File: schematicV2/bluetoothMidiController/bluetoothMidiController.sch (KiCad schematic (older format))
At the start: 24 parts, among them SW10 G1, SW11 G#1, SW12 A1, SW13 A#1, SW14 B1, SW15 PWR, SW16 C2, SW17 ALT, SW2 OCT+, SW20 OCT-, SW3 C1, SW4 C#1, SW5 D1, SW6 D#1, SW7 E1, SW8 F1, SW9 F#1

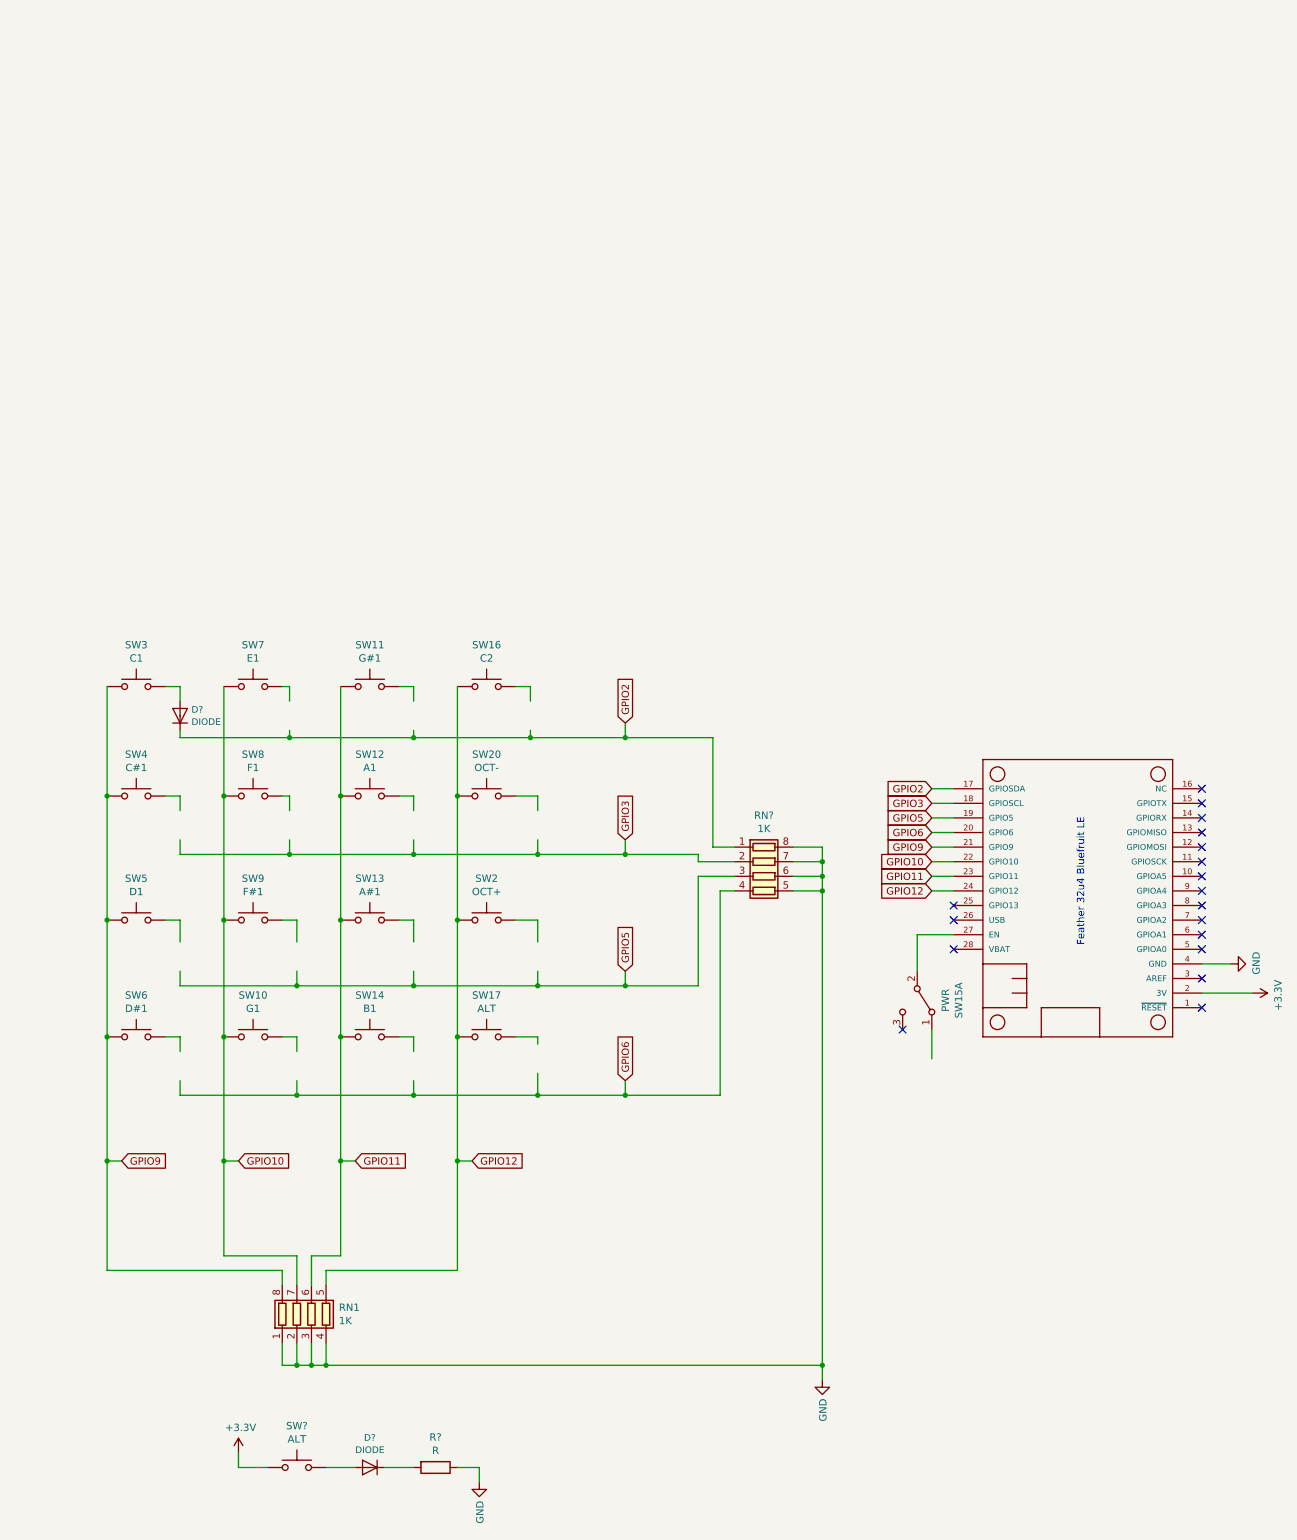
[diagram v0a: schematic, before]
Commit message: Added RGB LED support; started version 2 of board
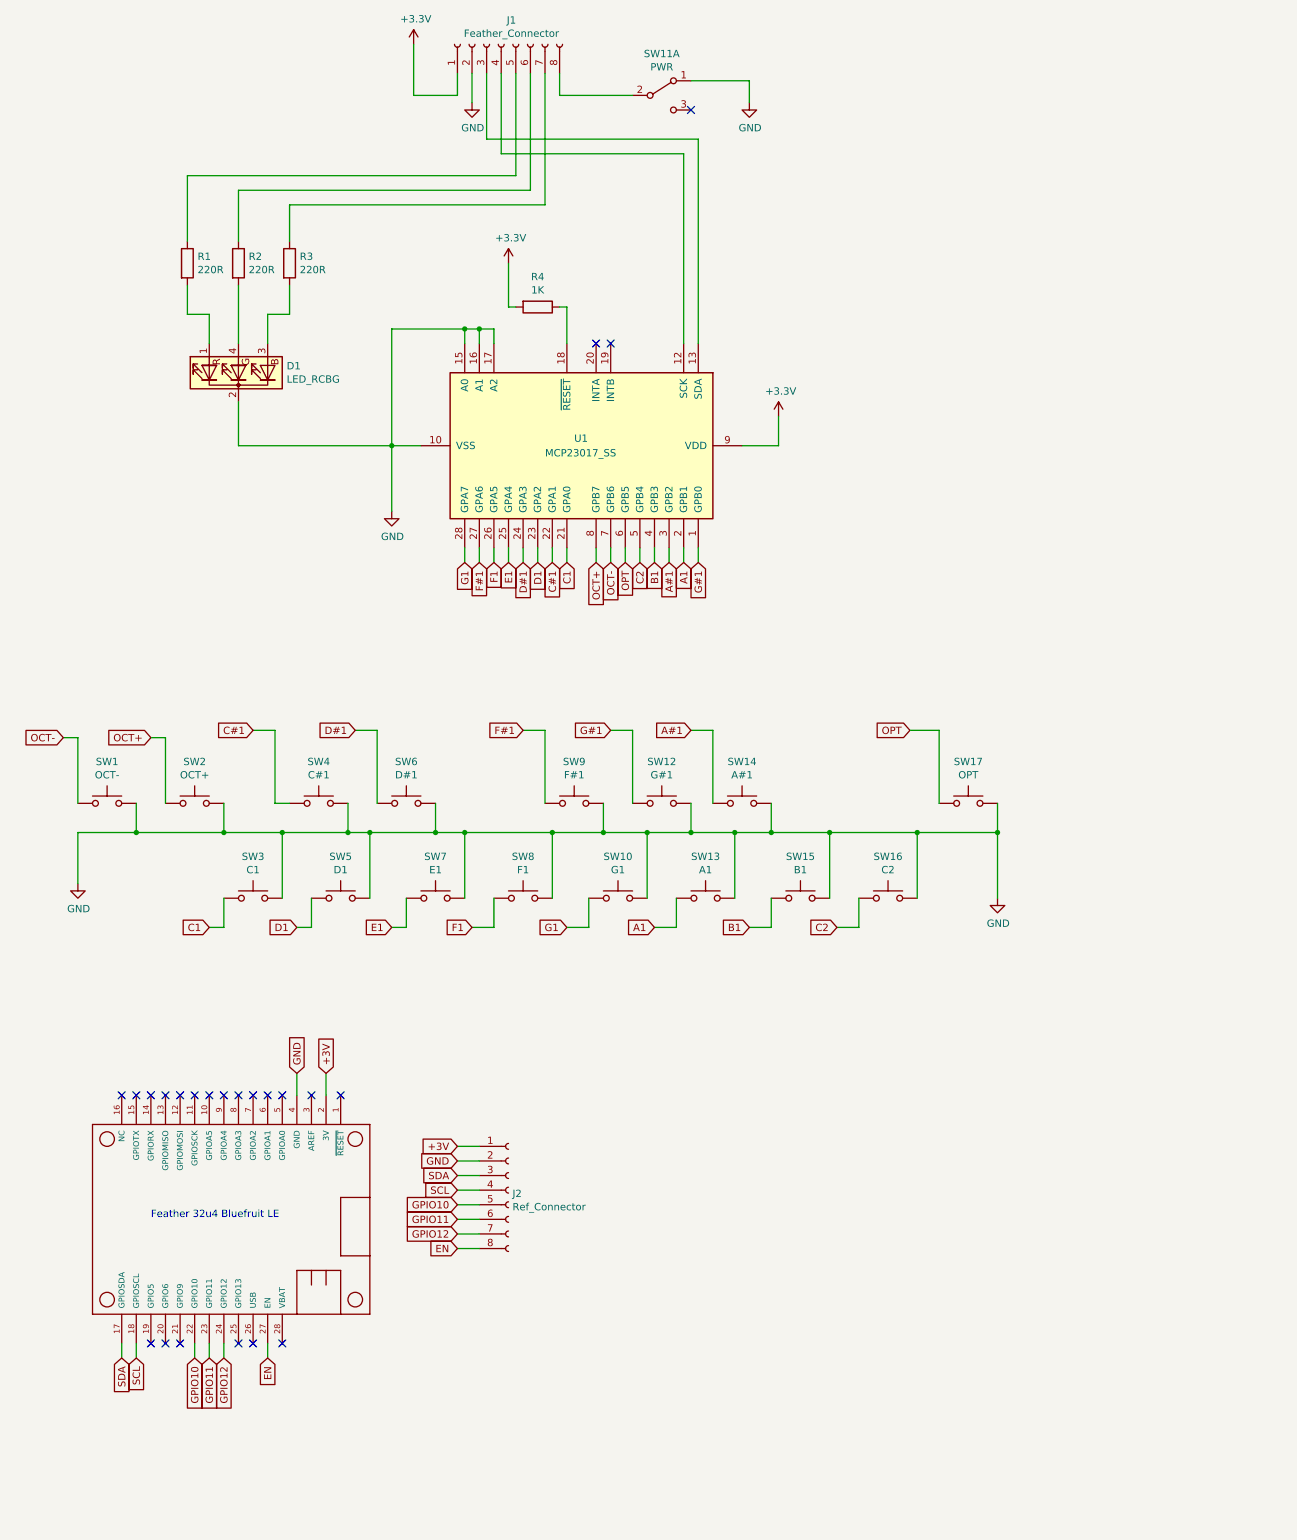
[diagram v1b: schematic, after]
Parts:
- removed D? (x2): DIODE, symbol adafruit:DIODE
- removed R?: R, symbol Device:R
- removed RN1: 1K, Resistor_SMD:R_Array_Convex_4x1206, symbol Device:R_Pack04
- removed RN?: 1K, symbol Device:R_Pack04
- removed SW20: OCT-, Button_Switch_THT:SW_PUSH-12mm, symbol Switch:SW_Push
- removed SW?: ALT, Button_Switch_THT:SW_PUSH-12mm, symbol Switch:SW_Push
- added D1: LED_RCBG, LED_THT:LED_D5.0mm-4_RGB, symbol Device:LED_RCBG
- added J1: Feather_Connector, Connector_PinHeader_2.54mm:PinHeader_1x08_P2.54mm_Vertical, symbol Connector:Conn_01x08_Female
- added J2: Ref_Connector, Connector_PinHeader_2.54mm:PinHeader_1x08_P2.54mm_Vertical, symbol Connector:Conn_01x08_Female
- added R1, R2, R3: 220R, Resistor_SMD:R_1206_3216Metric_Pad1.42x1.75mm_HandSolder, symbol Device:R
- added R4: 1K, Resistor_SMD:R_1206_3216Metric_Pad1.42x1.75mm_HandSolder, symbol Device:R
- added SW1: OCT-, Button_Switch_THT:SW_PUSH_6mm, symbol Switch:SW_Push
- added U1: MCP23017_SS, Package_SO:SSOP-28_5.3x10.2mm_P0.65mm, symbol Interface_Expansion:MCP23017_SS
- SW17: value ALT -> OPT
- renumbered SW15 to SW11, SW11 to SW12, SW12 to SW13, SW13 to SW14, SW14 to SW15
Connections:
- net labels added: +3V, A#1, A1, B1, C#1, C1, C2, D#1, D1, E1, EN, F#1, F1, G#1, G1, OCT+, OCT-, OPT, SCL, SDA
- net labels removed: GPIO2, GPIO3, GPIO5, GPIO6, GPIO9
- wire segments 148 -> 146
- no-connect marks 18 -> 23
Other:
- moved on the sheet: SW10, SW11A, SW12, SW13, SW14, SW15, SW16, SW2, SW3, SW4, SW5, SW6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
